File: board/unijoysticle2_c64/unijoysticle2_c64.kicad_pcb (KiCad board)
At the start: 4 copper layers, 62.5 x 56 mm, 62 parts, among them J1 USB_B_Micro, J2 PORT JOY #1, J3 PORT JOY #2, Q1 S8050, Q2 S8050, SW1 RESET, SW2 BOOT, SW3 MODE, SW4 SWAP, U1 ESP32-WROOM-32E, U2 AMS1117-3.3, U3 CH340C, U4 74HC05, U5 74HC05, U6 74HC05

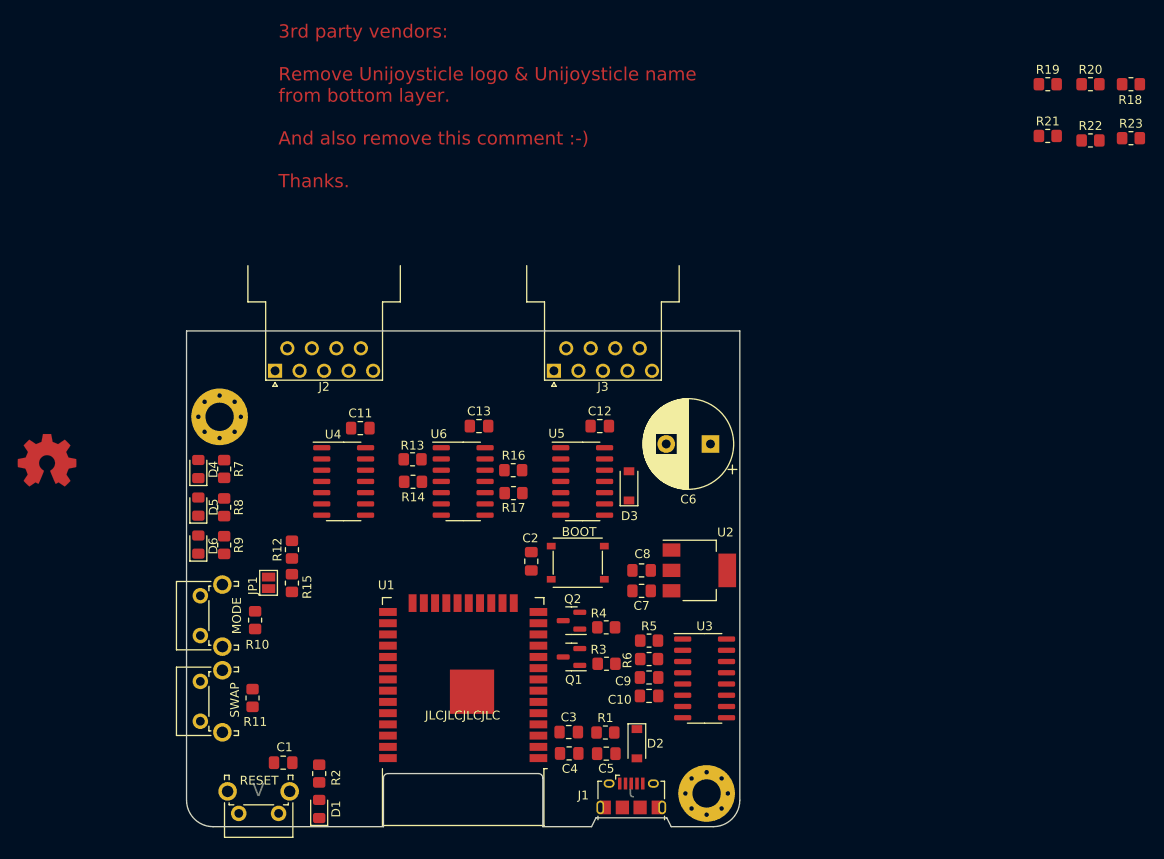
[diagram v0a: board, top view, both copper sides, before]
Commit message: c64: improved layout a bit.
board is a big larger, mounting hole better placed,
reset button moved to the left, and other layout improvements
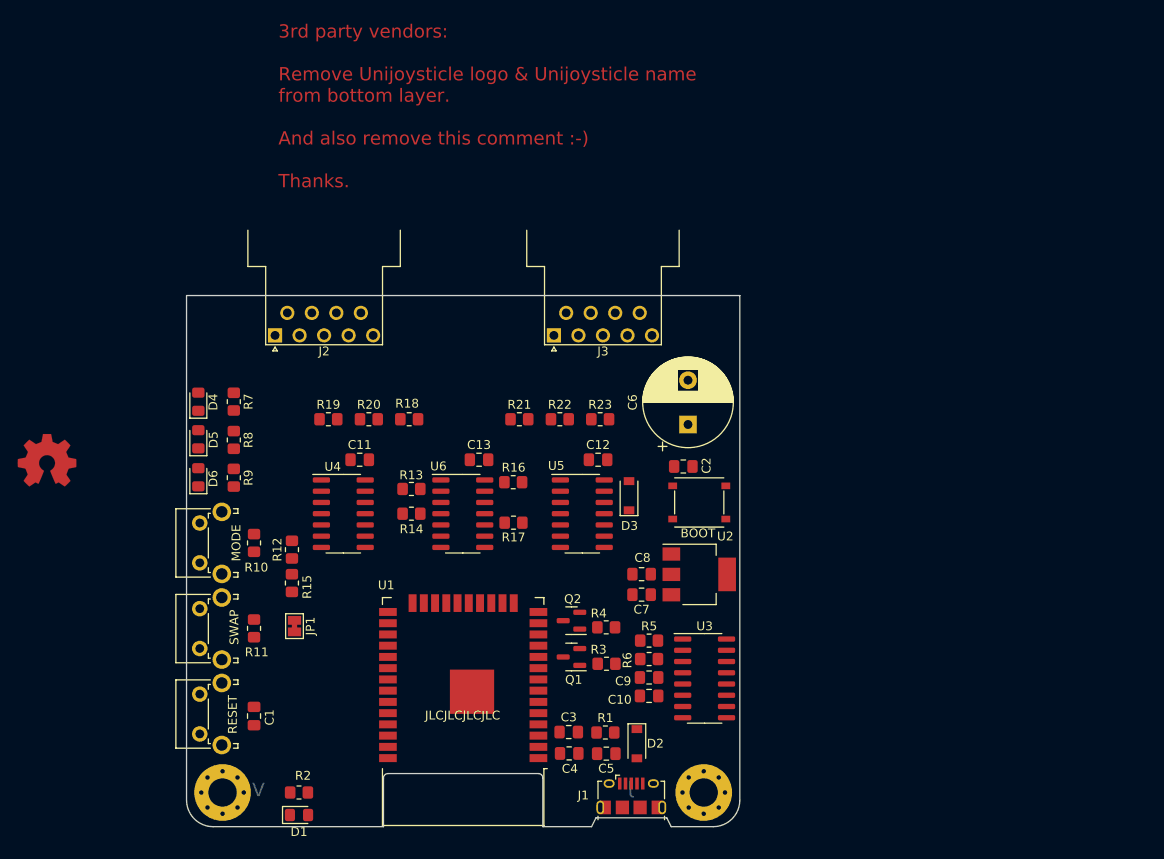
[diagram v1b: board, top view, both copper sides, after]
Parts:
- JP1: value SolderJumper_1_Open -> SolderJumper_2_Bridged; footprint Jumper:SolderJumper-2_P1.3mm_Open_Pad1.0x1.5mm -> Jumper:SolderJumper-2_P1.3mm_Bridged_Pad1.0x1.5mm
- moved R18 89.9 mm to (107.4, 104.0)
- moved R20 89.9 mm to (102.8, 104.0)
- moved R19 89.6 mm to (98.3, 104.0)
- moved R23 67.8 mm to (129.0, 104.0)
- moved R21 67.7 mm to (119.8, 104.0)
- moved R22 67.7 mm to (124.4, 104.0)
- moved H1 42.4 mm to (86.3, 146.1)
- moved C2 20.2 mm to (138.4, 109.3), turned to 180 degrees
- moved SW2 15.3 mm to (140.2, 113.4), turned to 180 degrees
- moved SW1 12.6 mm to (83.7, 139.5), turned to 90 degrees
- moved R10 8.72 mm to (89.9, 117.9)
- moved SW4 8.22 mm to (83.7, 129.9)
- moved SW3 8.22 mm to (83.7, 120.2)
- moved R11 7.86 mm to (89.9, 127.6)
- moved R7 7.68 mm to (87.6, 102.0)
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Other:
- board size 62.5 x 56 mm -> 62.5 x 60 mm

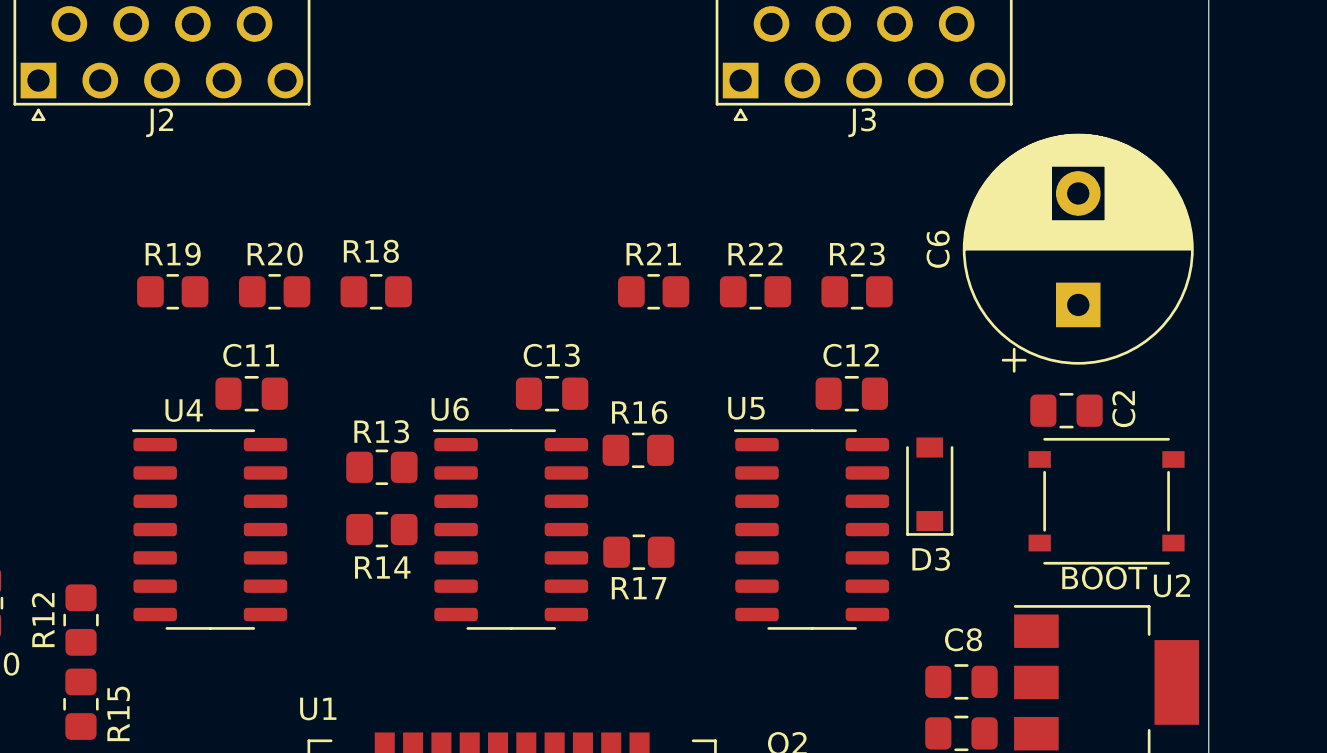
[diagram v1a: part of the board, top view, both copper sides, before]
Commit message: c64: back to using SMD cap for 2200uf
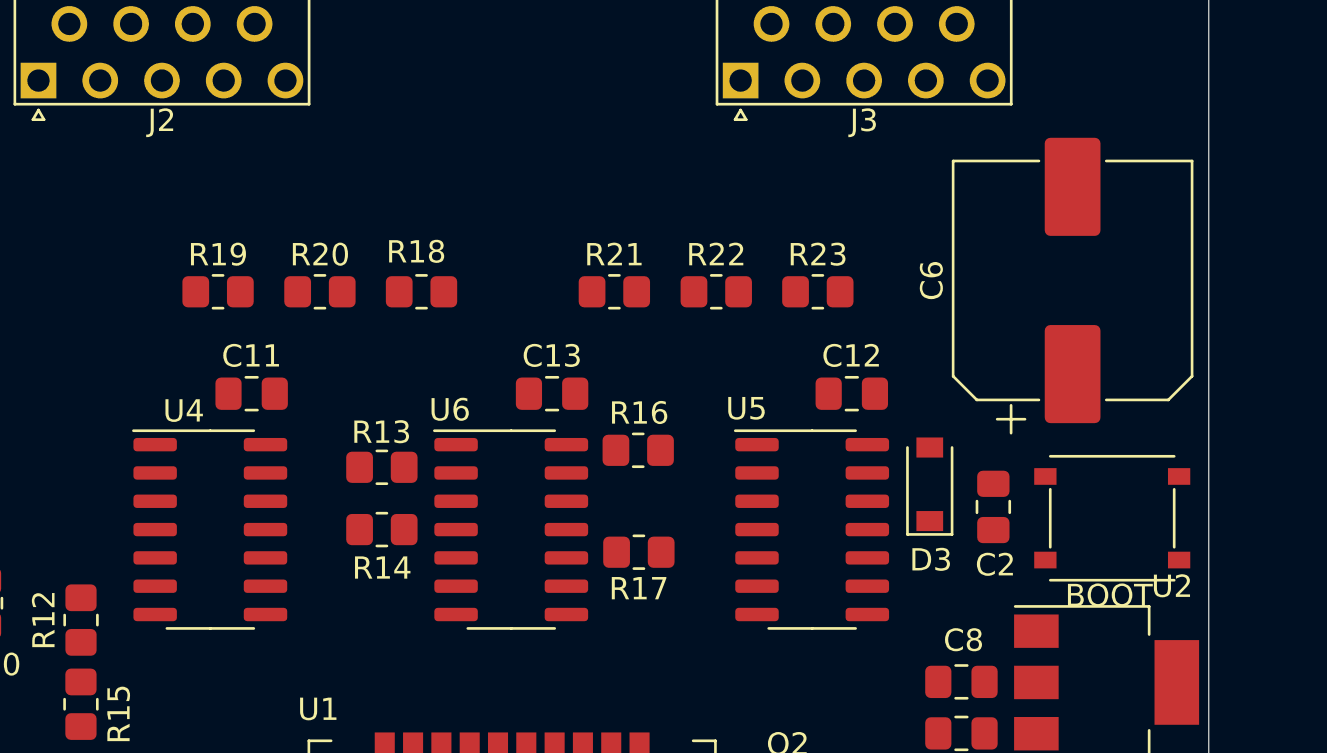
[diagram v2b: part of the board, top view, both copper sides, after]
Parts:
- C6: footprint Capacitor_THT:CP_Radial_D10.0mm_P5.00mm -> Capacitor_SMD:CP_Elec_10x10.5
- moved C2 5.42 mm to (135.1, 113.6), turned to 90 degrees
- moved R18 2.03 mm to (109.4, 104.0)
- moved R19 2.03 mm to (100.3, 104.0)
- moved R20 2.03 mm to (104.9, 104.0)
- moved R21 1.76 mm to (118.1, 104.0)
- moved R22 1.76 mm to (122.7, 104.0)
- moved R23 1.76 mm to (127.2, 104.0)
- moved C6 1.13 mm to (138.6, 103.5)
- moved SW2 0.80 mm to (140.4, 114.1)
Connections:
- net Net-(C6-Pad1) renamed /USB Serial & Power/+5V_FILTERED

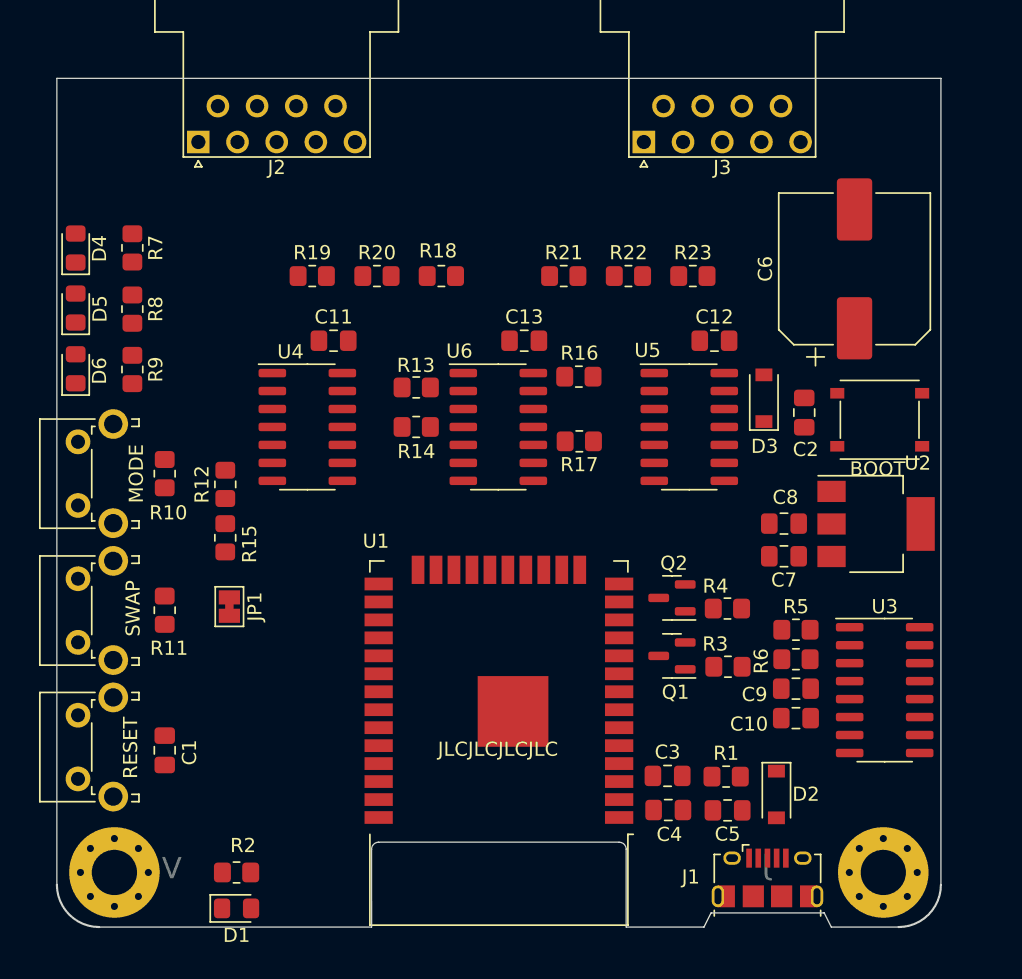
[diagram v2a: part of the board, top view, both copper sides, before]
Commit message: c64: layout improvements
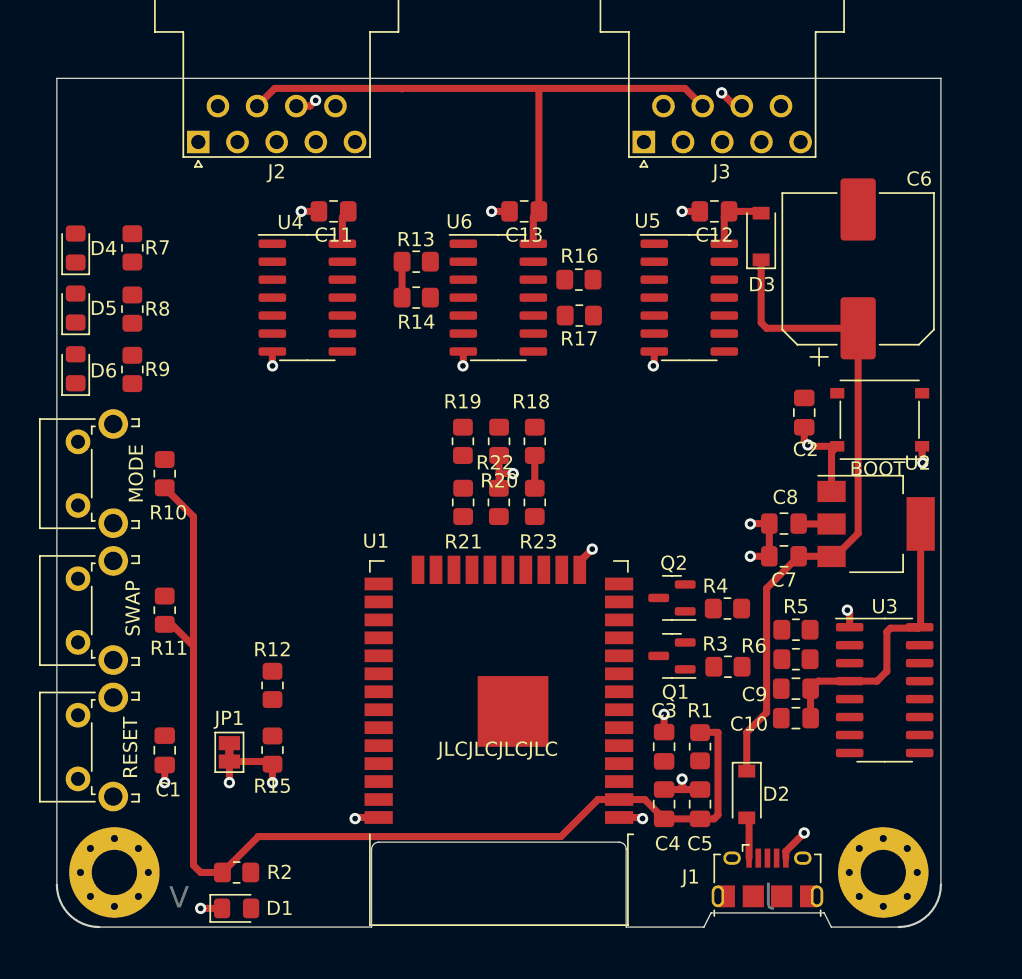
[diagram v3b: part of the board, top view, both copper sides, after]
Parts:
- moved R23 19.5 mm to (116.0, 120.0), turned to -90 degrees
- moved R22 18.4 mm to (113.5, 120.0), turned to 90 degrees
- moved R21 17.5 mm to (111.0, 120.0), turned to -90 degrees
- moved R19 15.8 mm to (111.0, 115.7), turned to 90 degrees
- moved R15 15.4 mm to (97.5, 137.5)
- moved R12 14.6 mm to (97.5, 132.9)
- moved R20 14.5 mm to (113.5, 115.7), turned to -90 degrees
- moved R18 13.4 mm to (116.0, 115.7), turned to 90 degrees
- moved D3 11.4 mm to (132.0, 101.2)
- moved JP1 10.3 mm to (94.4, 137.6), turned to 90 degrees
- moved C11 9.14 mm to (101.8, 99.4), turned to 180 degrees
- moved C12 9.14 mm to (128.7, 99.4), turned to 180 degrees
- moved C13 9.14 mm to (115.3, 99.4), turned to 180 degrees
- moved R14 9.14 mm to (107.7, 105.5)
- moved U4 9.14 mm to (100.0, 105.5)
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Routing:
- net +3V3: track 0.00 -> 102.6 mm
- net +5V: track 0.00 -> 53.5 mm
- net GND: track 0.00 -> 48.7 mm, vias 0 -> 24
- net /USB Serial & Power/+5V_FILTERED: track 0.00 -> 47.6 mm
- net VBUS: track 0.00 -> 2.92 mm

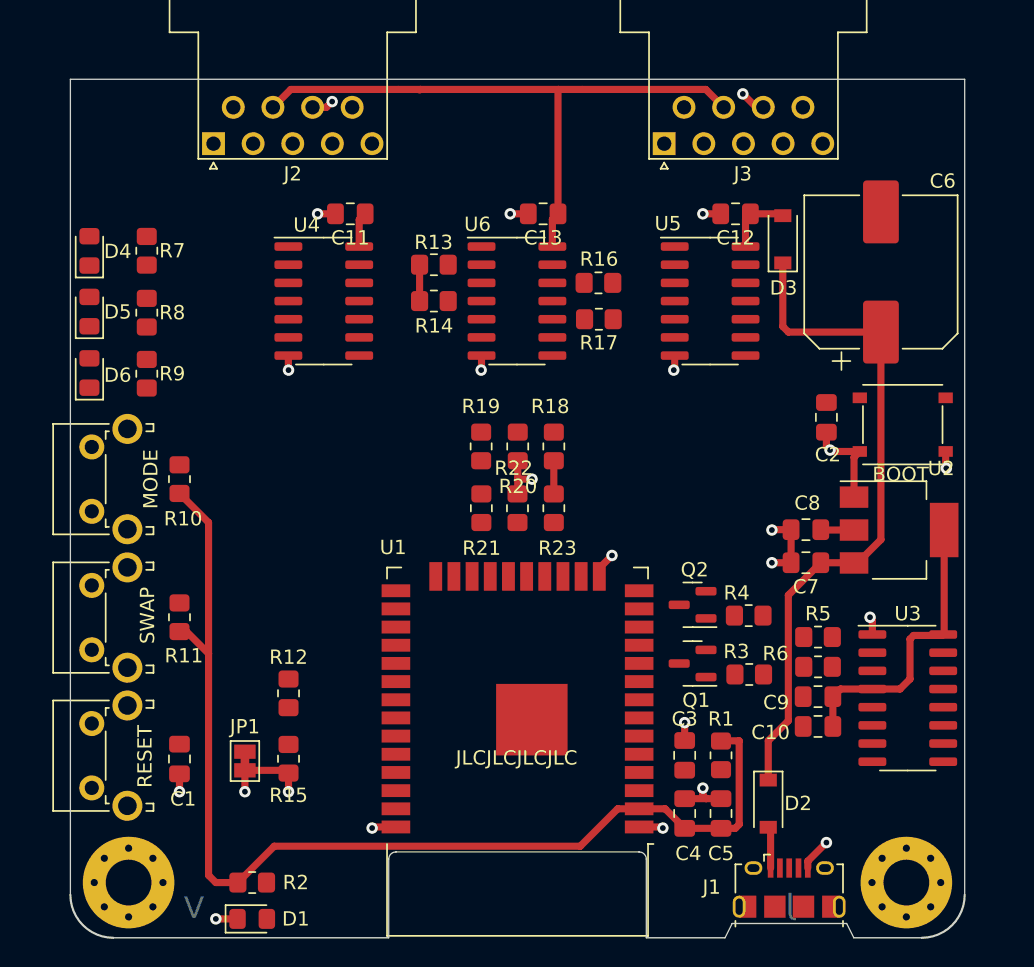
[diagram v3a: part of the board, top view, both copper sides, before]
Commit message: c64: more progress on routing
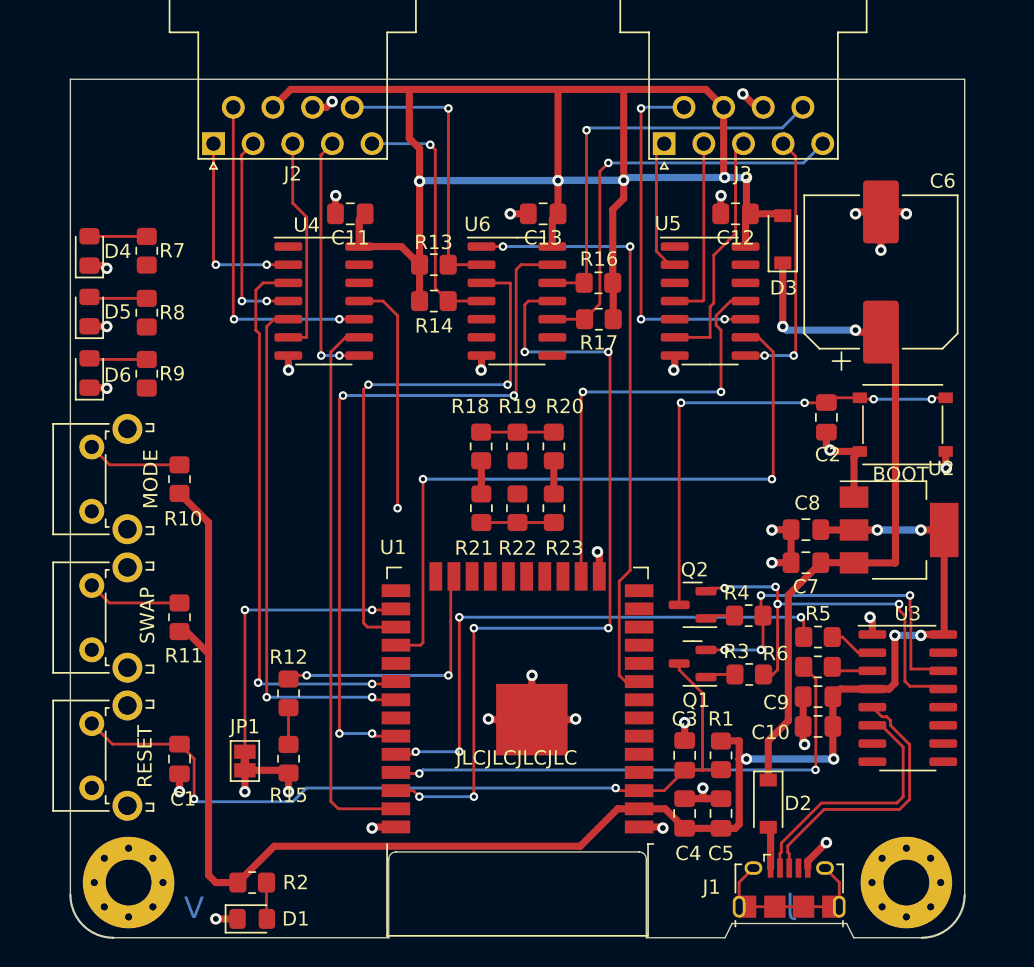
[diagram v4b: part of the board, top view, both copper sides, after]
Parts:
- R21: value 1.7K -> 10K
- R22: value 3.3K -> 1.7K
- R23: value 10K -> 3.3K
- moved R18 5.08 mm to (111.0, 115.7)
- moved R19 2.54 mm to (113.5, 115.7)
- moved R20 2.52 mm to (116.0, 115.7)
- turned R22 to -90 degrees
- turned R23 to 90 degrees
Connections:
- net Net-(D1-Pad2) renamed /ESP32/+3V3_LED
- R21 pad 1: /C64 Ports/J2_POTY -> +3V3
- R22 pad 1: GPIO_39 -> /C64 Ports/J2_POTY
- R22 pad 2: GND -> GPIO_39
- R23 pad 1: +3V3 -> GPIO_39
- R23 pad 2: GPIO_39 -> GND
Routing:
- net +5V: track 53.5 -> 117.7 mm, vias 0 -> 5
- net GPIO_J2_POTY: track 0.00 -> 57.4 mm, vias 0 -> 6
- net /ESP32/ESP_EN: track 0.00 -> 57.1 mm, vias 0 -> 2
- net GPIO_J2_POTX: track 0.00 -> 51.3 mm, vias 0 -> 4
- net GPIO_J2_RIGHT: track 0.00 -> 49.1 mm, vias 0 -> 2
- net GPIO_J1_POTX: track 0.00 -> 42.2 mm, vias 0 -> 2
- net GPIO_J1_DOWN: track 0.00 -> 39.8 mm, vias 0 -> 2
- net UART_TX: track 0.00 -> 39.2 mm, vias 0 -> 4
- net GPIO_J1_RIGHT: track 0.00 -> 38.6 mm
- net GPIO_J1_POTY: track 0.00 -> 38.2 mm, vias 0 -> 2
- net UART_RX: track 0.00 -> 37.0 mm, vias 0 -> 2
- net GPIO_J1_LEFT: track 0.00 -> 36.7 mm, vias 0 -> 2
- net /ESP32/ESP_BOOT: track 0.00 -> 32.9 mm, vias 0 -> 4
- net GPIO_J2_FIRE: track 0.00 -> 30.6 mm, vias 0 -> 2
- net /C64 Ports/J2_POTY: track 0.00 -> 29.4 mm, vias 0 -> 1
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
